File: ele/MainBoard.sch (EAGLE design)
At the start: 58 parts, among them X1 M8, X2 M8, X4 POWER_IN

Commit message: fix
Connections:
- new net GPIO33_5V: IM11.HIGH3, JP1.3
- net GPIO32_5V: no longer IM11.HIGH3, JP1.3
- net PWM2: no longer IM6.IO16
- net PWM3: now also IM6.IO16
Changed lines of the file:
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@@
 <net name="GPIO32_5V" class="0">
-<segment>
-<pinref part="IM11" gate="G$1" pin="HIGH3"/>
-<wire x1="264.16" y1="129.54" x2="289.56" y2="129.54" width="0.1524" layer="91"/>
-<label x="271.78" y="129.54" size="1.778" layer="95"/>
-<pinref part="JP1" gate="A" pin="3"/>
-</segment>
 <segment>
 <pinref part="IM11" gate="G$1" pin="HIGH4"/>
@@
 <junction x="106.68" y="200.66"/>
 </segment>
-<segment>
-<pinref part="IM6" gate="G$1" pin="IO16"/>
-<wire x1="96.52" y1="195.58" x2="106.68" y2="195.58" width="0.1524" layer="91"/>
-<label x="96.52" y="195.58" size="1.778" layer="95"/>
-<junction x="106.68" y="195.58"/>
-</segment>
 </net>
 <net name="N$4" class="0">
@@
 </segment>
 </net>
+<net name="PWM3" class="0">
+<segment>
+<pinref part="IM6" gate="G$1" pin="IO16"/>
+<wire x1="96.52" y1="195.58" x2="106.68" y2="195.58" width="0.1524" layer="91"/>
+<label x="96.52" y="195.58" size="1.778" layer="95"/>
+<junction x="106.68" y="195.58"/>
+</segment>
+</net>
+<net name="GPIO33_5V" class="0">
+<segment>
+<pinref part="IM11" gate="G$1" pin="HIGH3"/>
+<wire x1="264.16" y1="129.54" x2="289.56" y2="129.54" width="0.1524" layer="91"/>
+<label x="271.78" y="129.54" size="1.778" layer="95"/>
+<pinref part="JP1" gate="A" pin="3"/>
+</segment>
+</net>

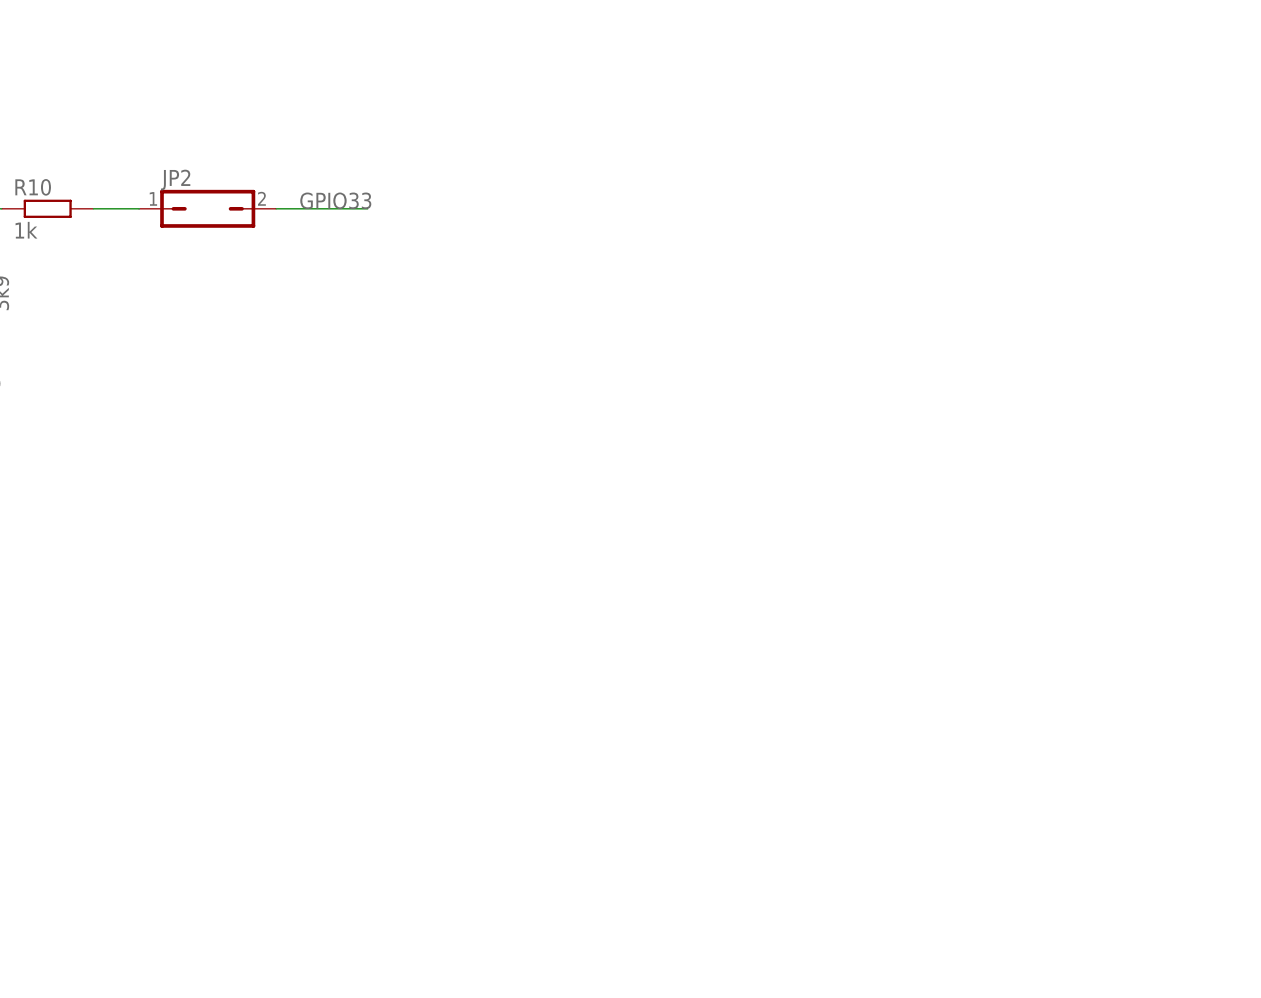
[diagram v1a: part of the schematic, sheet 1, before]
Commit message: ele: MainBoard - Add CC BY-SA license, fix pinheads position
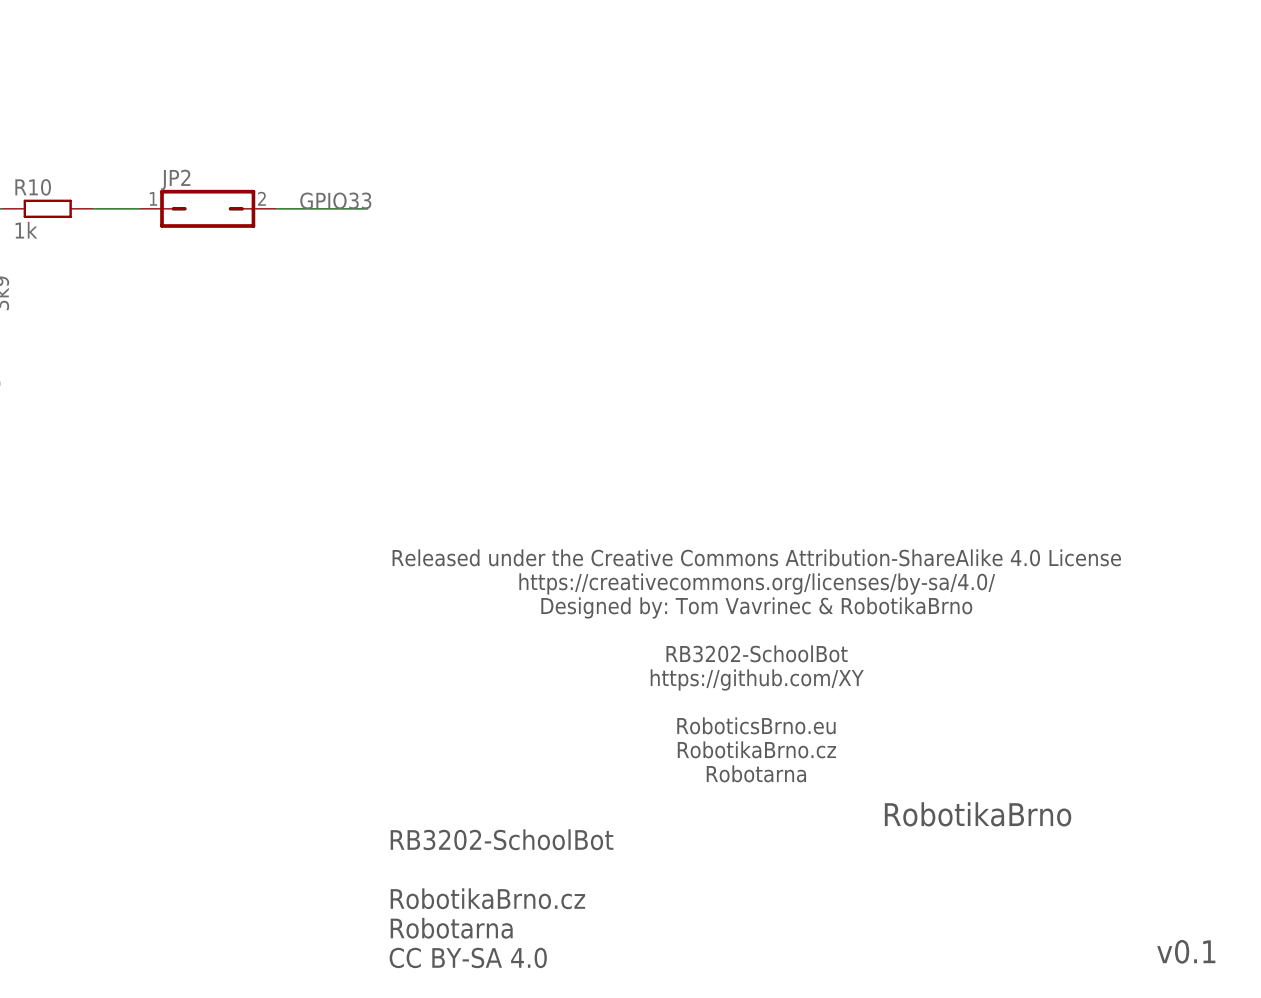
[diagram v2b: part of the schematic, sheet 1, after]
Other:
- note added: "RB3202-SchoolBot RobotikaBrno.cz Robotarna CC BY-SA 4.0"
- note added: "Released under the Creative Commons Attribution-ShareAlike 4.0 License https://creativecommons.org/licenses/by-sa/4.0/ Designed by: Tom Vavrinec & RobotikaBrno RB3202-SchoolBot https://github.com/XY RoboticsBrno.eu RobotikaBrno.cz Robotarna"
- note added: "RobotikaBrno"
- note added: "v0.1"

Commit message: condenser
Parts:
- added C7: (no value), rcl:CPOL-EUE5-10.5
- added D3: (no value), diode:SCHOTTKY-DIODEF126Z12
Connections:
- removed net N$7: IM3.EN
- net GND: now also C7.-, D3.A
- net IO9_NC2: now also IM3.EN
- net VCC: now also C7.+, D3.C
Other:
- moved on the sheet: IM3, IM4, J2, JP10, JP12, JP14

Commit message: ladeni
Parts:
- added C6: (no value), rcl:CPOL-EUE5-10.5
- added JP7: (no value), pinhead:PINHD-1X4/90
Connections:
- net +5V: now also JP7.1, JP7.2, JP7.3, JP7.4
- net GND: now also C6.-
- net VCC: now also C6.+
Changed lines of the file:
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@@
 <part name="GND55" library="supply1" library_urn="urn:adsk.eagle:library:371" deviceset="GND" device=""/>
 <part name="C7" library="rcl" library_urn="urn:adsk.eagle:library:334" deviceset="CPOL-EU" device="E5-10.5" package3d_urn="urn:adsk.eagle:package:23372/1"/>
+<part name="GND27" library="supply1" library_urn="urn:adsk.eagle:library:371" deviceset="GND" device=""/>
+<part name="P+8" library="supply1" library_urn="urn:adsk.eagle:library:371" deviceset="VCC" device=""/>
+<part name="C6" library="rcl" library_urn="urn:adsk.eagle:library:334" deviceset="CPOL-EU" device="E5-10.5" package3d_urn="urn:adsk.eagle:package:23372/1"/>
+<part name="JP7" library="pinhead" library_urn="urn:adsk.eagle:library:325" deviceset="PINHD-1X4" device="/90" package3d_urn="urn:adsk.eagle:package:22404/2"/>
+<part name="P+11" library="supply1" library_urn="urn:adsk.eagle:library:371" deviceset="+5V" device=""/>
 </parts>
 <sheets>
@@
 <attribute name="VALUE" x="285.75" y="121.92" size="1.778" layer="96"/>
 </instance>
+<instance part="JP7" gate="A" x="325.12" y="129.54" smashed="yes">
+<attribute name="NAME" x="318.77" y="137.795" size="1.778" layer="95"/>
+<attribute name="VALUE" x="318.77" y="121.92" size="1.778" layer="96"/>
+</instance>
+<instance part="P+11" gate="1" x="312.42" y="144.78" smashed="yes">
+<attribute name="VALUE" x="309.88" y="139.7" size="1.778" layer="96" rot="R90"/>
+</instance>
 </instances>
 <busses>
@@
 <pinref part="P+10" gate="1" pin="+5V"/>
 </segment>
+<segment>
+<pinref part="JP7" gate="A" pin="4"/>
+<wire x1="322.58" y1="127" x2="312.42" y2="127" width="0.1524" layer="91"/>
+<wire x1="312.42" y1="127" x2="312.42" y2="129.54" width="0.1524" layer="91"/>
+<pinref part="JP7" gate="A" pin="3"/>
+<wire x1="312.42" y1="129.54" x2="312.42" y2="132.08" width="0.1524" layer="91"/>
+<wire x1="312.42" y1="132.08" x2="312.42" y2="134.62" width="0.1524" layer="91"/>
+<wire x1="312.42" y1="134.62" x2="312.42" y2="142.24" width="0.1524" layer="91"/>
+<wire x1="322.58" y1="129.54" x2="312.42" y2="129.54" width="0.1524" layer="91"/>
+<junction x="312.42" y="129.54"/>
+<pinref part="JP7" gate="A" pin="2"/>
+<wire x1="312.42" y1="132.08" x2="322.58" y2="132.08" width="0.1524" layer="91"/>
+<junction x="312.42" y="132.08"/>
+<pinref part="JP7" gate="A" pin="1"/>
+<wire x1="322.58" y1="134.62" x2="312.42" y2="134.62" width="0.1524" layer="91"/>
+<junction x="312.42" y="134.62"/>
+<pinref part="P+11" gate="1" pin="+5V"/>
+</segment>
 </net>
 <net name="+3V3" class="0">
@@
 <attribute name="VALUE" x="265.303" y="84.3026" size="1.778" layer="96"/>
 </instance>
+<instance part="GND27" gate="1" x="254" y="76.2" smashed="yes">
+<attribute name="VALUE" x="251.46" y="73.66" size="1.778" layer="96"/>
+</instance>
+<instance part="P+8" gate="VCC" x="254" y="101.6" smashed="yes">
+<attribute name="VALUE" x="256.54" y="99.06" size="1.778" layer="96"/>
+</instance>
+<instance part="C6" gate="G$1" x="254" y="88.9" smashed="yes">
+<attribute name="NAME" x="255.143" y="89.3826" size="1.778" layer="95"/>
+<attribute name="VALUE" x="255.143" y="84.3026" size="1.778" layer="96"/>
+</instance>
 </instances>
 <busses>
@@
 <wire x1="276.86" y1="78.74" x2="276.86" y2="86.36" width="0.1524" layer="91"/>
 </segment>
+<segment>
+<wire x1="254" y1="83.82" x2="254" y2="78.74" width="0.1524" layer="91"/>
+<pinref part="GND27" gate="1" pin="GND"/>
+<pinref part="C6" gate="G$1" pin="-"/>
+</segment>
 </net>
 <net name="+5V" class="0">
@@
 <wire x1="276.86" y1="91.44" x2="276.86" y2="99.06" width="0.1524" layer="91"/>
 </segment>
+<segment>
+<wire x1="254" y1="91.44" x2="254" y2="99.06" width="0.1524" layer="91"/>
+<pinref part="P+8" gate="VCC" pin="VCC"/>
+<pinref part="C6" gate="G$1" pin="+"/>
+</segment>
 </net>
